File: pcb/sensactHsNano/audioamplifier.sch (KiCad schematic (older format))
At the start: 26 parts, among them U1 TAS5805M

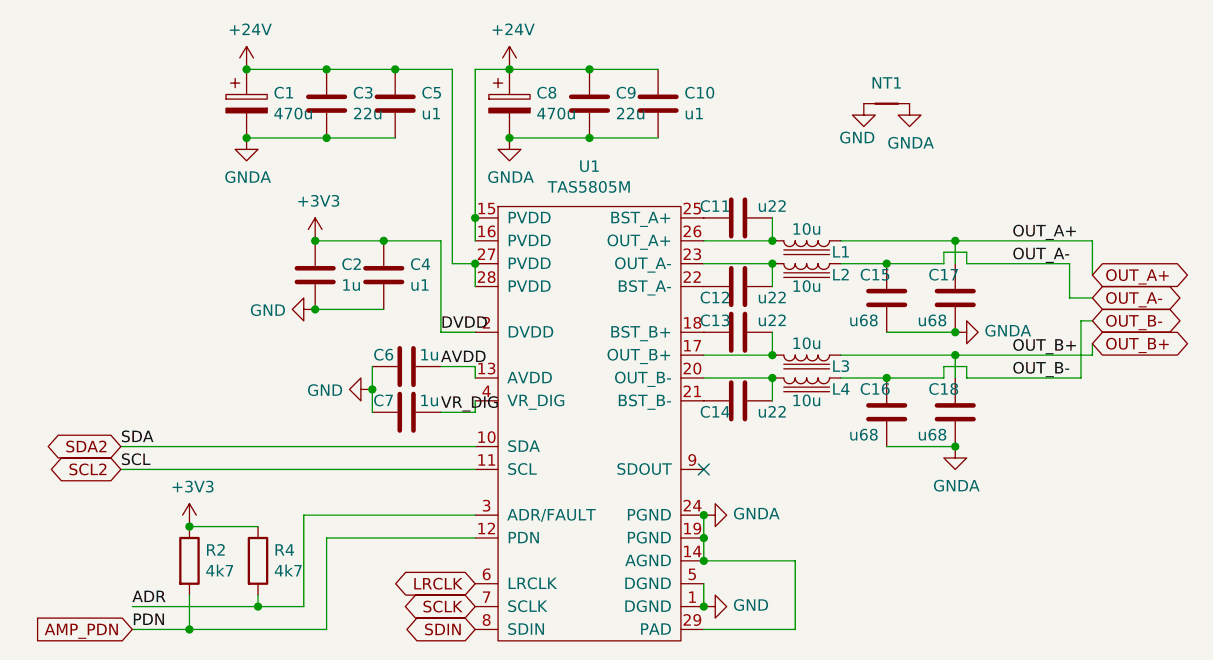
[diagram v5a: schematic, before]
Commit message: sensactHsNano for Reflow Soldering
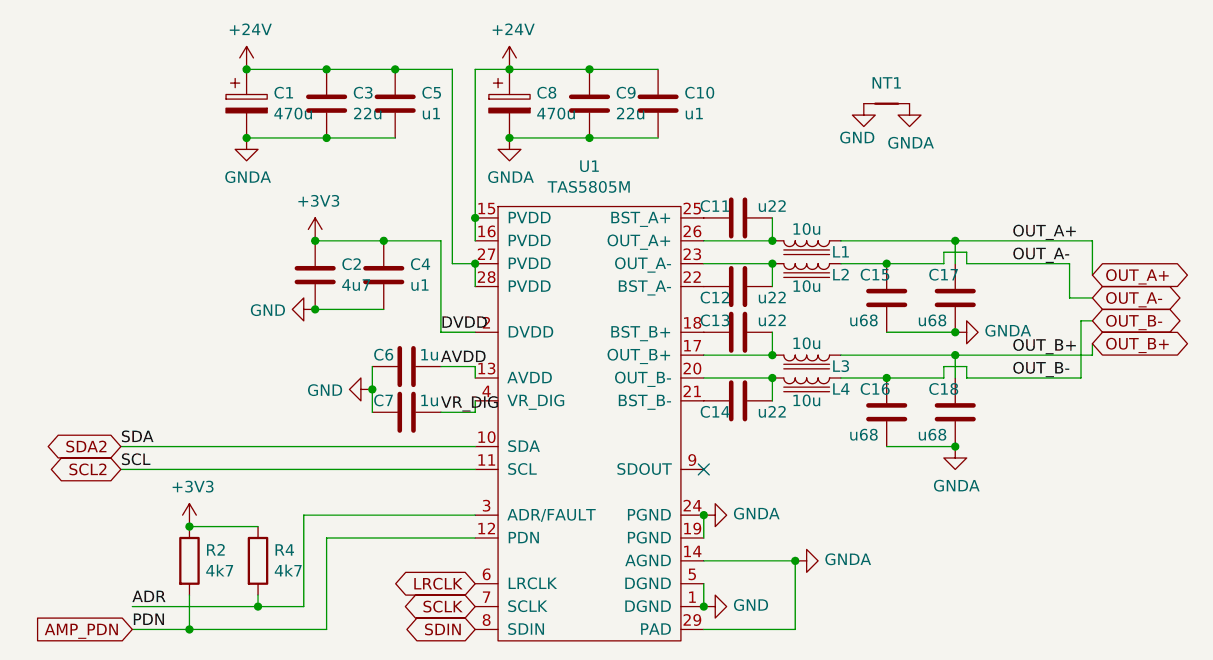
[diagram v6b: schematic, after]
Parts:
- removed U1: TAS5805M, sensact:TSSOP-28_4.4x9.7mm_Pitch0.65mm_pad_handsolder, symbol sensactHsNano-rescue:TAS5805M-sensact
- added U1: TAS5805M, Package_SO:HTSSOP-28-1EP_4.4x9.7mm_P0.65mm_EP2.85x5.4mm_ThermalVias, symbol liebler_SEMICONDUCTORS:TAS5805M
- C10, C11, C12, C13, C14, C4, C5, C6, C7: footprint Capacitor_SMD:C_0805_2012Metric_Pad1.18x1.45mm_HandSolder -> Capacitor_SMD:C_0603_1608Metric
- C2: value 1u -> 4u7; footprint Capacitor_SMD:C_0805_2012Metric_Pad1.18x1.45mm_HandSolder -> Capacitor_SMD:C_0603_1608Metric
- C3, C9: footprint Capacitor_SMD:C_1206_3216Metric_Pad1.33x1.80mm_HandSolder -> Capacitor_SMD:C_1206_3216Metric
- L1, L2, L3, L4: footprint liebler_PASSIVES:Inductor_CDRH104_handsolder -> liebler_PASSIVES:L_1040
- R4: footprint Resistor_SMD:R_0805_2012Metric_Pad1.20x1.40mm_HandSolder -> Resistor_SMD:R_0603_1608Metric
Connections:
- net +24V: now also U1.15 (PVDD), U1.16 (PVDD), U1.27 (PVDD), U1.28 (PVDD)
- net +3V3: now also U1.2 (DVDD)
- net ADR: now also U1.3 (ADR/FAULT)
- net AMP_PDN: now also U1.12 (PDN)
- net AVDD: now also U1.13 (AVDD)
- net GND: now also U1.1 (DGND), U1.5 (DGND)
- net GNDA: now also U1.14 (AGND), U1.19 (PGND), U1.24 (PGND), U1.29 (PAD)
- net LRCLK: now also U1.6 (LRCLK)
- net SCL2: now also U1.11 (SCL)
- net SCLK: now also U1.7 (SCLK)
- net SDA2: now also U1.10 (SDA)
- net SDIN: now also U1.8 (SDIN)
- net VR_DIG: now also U1.4 (VR_DIG)
- net at C11.1, L1.2: now also U1.26 (OUT_A+)
- net at C13.1, L3.2: now also U1.17 (OUT_B+)
- net at C13.2: now also U1.18 (BST_B+)
- net at C14.1, L4.2: now also U1.20 (OUT_B-)
- net at C14.2: now also U1.21 (BST_B-)
- net at C12.2: now also U1.22 (BST_A-)
- net at C12.1, L2.2: now also U1.23 (OUT_A-)
- net at C11.2: now also U1.25 (BST_A+)
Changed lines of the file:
@@
 F 0 "L1" V 5300 2300 50  0000 C CNN
 F 1 "10u" V 5200 2150 50  0000 C CNN
-F 2 "liebler_PASSIVES:Inductor_CDRH104_handsolder" H 5250 2150 50  0001 C CNN
+F 2 "liebler_PASSIVES:L_1040" H 5250 2150 50  0001 C CNN
 F 3 "~" H 5250 2150 50  0001 C CNN
 	1    5250 2150
 	0    1    1    0
-$EndComp
-$Comp
-L sensactHsNano-rescue:TAS5805M-sensact U1
-U 1 1 5F9CF512
-P 4300 2950
-F 0 "U1" H 4300 4075 50  0000 C CNN
-F 1 "TAS5805M" H 4300 3984 50  0000 C CNN
-F 2 "sensact:TSSOP-28_4.4x9.7mm_Pitch0.65mm_pad_handsolder" H 4300 3450 50  0001 C CNN
-F 3 "" H 4300 3450 50  0001 C CNN
-	1    4300 2950
-	1    0    0    -1
 $EndComp
 $Comp
@@
 F 0 "C11" V 4900 1950 50  0000 C CNN
 F 1 "u22" V 4900 2200 50  0000 C CNN
-F 2 "Capacitor_SMD:C_0805_2012Metric_Pad1.18x1.45mm_HandSolder" H 4988 1900 50  0001 C CNN
+F 2 "Capacitor_SMD:C_0603_1608Metric" H 4988 1900 50  0001 C CNN
 F 3 "~" H 4950 2050 50  0001 C CNN
 	1    4950 2050
@@
 F 0 "L2" V 5300 2400 50  0000 C CNN
 F 1 "10u" V 5350 2250 50  0000 C CNN
-F 2 "liebler_PASSIVES:Inductor_CDRH104_handsolder" H 5250 2250 50  0001 C CNN
+F 2 "liebler_PASSIVES:L_1040" H 5250 2250 50  0001 C CNN
 F 3 "~" H 5250 2250 50  0001 C CNN
 	1    5250 2250
@@
 F 0 "C12" V 5000 2250 50  0000 C CNN
 F 1 "u22" V 5000 2500 50  0000 C CNN
-F 2 "Capacitor_SMD:C_0805_2012Metric_Pad1.18x1.45mm_HandSolder" H 4988 2200 50  0001 C CNN
+F 2 "Capacitor_SMD:C_0603_1608Metric" H 4988 2200 50  0001 C CNN
 F 3 "~" H 4950 2350 50  0001 C CNN
 	1    4950 2350
@@
 F 0 "L3" V 5300 2800 50  0000 C CNN
 F 1 "10u" V 5200 2650 50  0000 C CNN
-F 2 "liebler_PASSIVES:Inductor_CDRH104_handsolder" H 5250 2650 50  0001 C CNN
+F 2 "liebler_PASSIVES:L_1040" H 5250 2650 50  0001 C CNN
 F 3 "~" H 5250 2650 50  0001 C CNN
 	1    5250 2650
@@
 F 0 "C13" V 4900 2450 50  0000 C CNN
 F 1 "u22" V 4900 2700 50  0000 C CNN
-F 2 "Capacitor_SMD:C_0805_2012Metric_Pad1.18x1.45mm_HandSolder" H 4988 2400 50  0001 C CNN
+F 2 "Capacitor_SMD:C_0603_1608Metric" H 4988 2400 50  0001 C CNN
 F 3 "~" H 4950 2550 50  0001 C CNN
 	1    4950 2550
@@
 F 0 "L4" V 5300 2900 50  0000 C CNN
 F 1 "10u" V 5350 2750 50  0000 C CNN
-F 2 "liebler_PASSIVES:Inductor_CDRH104_handsolder" H 5250 2750 50  0001 C CNN
+F 2 "liebler_PASSIVES:L_1040" H 5250 2750 50  0001 C CNN
 F 3 "~" H 5250 2750 50  0001 C CNN
 	1    5250 2750
@@
 F 0 "C14" V 5000 2750 50  0000 C CNN
 F 1 "u22" V 5000 3000 50  0000 C CNN
-F 2 "Capacitor_SMD:C_0805_2012Metric_Pad1.18x1.45mm_HandSolder" H 4988 2700 50  0001 C CNN
+F 2 "Capacitor_SMD:C_0603_1608Metric" H 4988 2700 50  0001 C CNN
 F 3 "~" H 4950 2850 50  0001 C CNN
 	1    4950 2850
@@
 	5100 2850 5100 2750
 Connection ~ 5100 2750
-$Comp
-L Device:C C15
-U 1 1 5F9D60B0
-P 5600 2400
-F 0 "C15" H 5650 2300 50  0000 C CNN
-F 1 "u68" H 5700 2500 50  0000 C CNN
-F 2 "Capacitor_SMD:C_1206_3216Metric_Pad1.33x1.80mm_HandSolder" H 5638 2250 50  0001 C CNN
-F 3 "~" H 5600 2400 50  0001 C CNN
-	1    5600 2400
-	-1   0    0    1
-$EndComp
-$Comp
-L Device:C C17
-U 1 1 5F9D6EDC
-P 5900 2400
-F 0 "C17" H 5950 2300 50  0000 C CNN
-F 1 "u68" H 6000 2500 50  0000 C CNN
-F 2 "Capacitor_SMD:C_1206_3216Metric_Pad1.33x1.80mm_HandSolder" H 5938 2250 50  0001 C CNN
-F 3 "~" H 5900 2400 50  0001 C CNN
-	1    5900 2400
-	-1   0    0    1
-$EndComp
 Wire Wire Line
 	5400 2250 5600 2250
@@
 Wire Wire Line
 	5600 2550 5900 2550
-$Comp
-L Device:C C16
-U 1 1 5F9D93BD
-P 5600 2900
-F 0 "C16" H 5650 2800 50  0000 C CNN
-F 1 "u68" H 5700 3000 50  0000 C CNN
-F 2 "Capacitor_SMD:C_1206_3216Metric_Pad1.33x1.80mm_HandSolder" H 5638 2750 50  0001 C CNN
-F 3 "~" H 5600 2900 50  0001 C CNN
-	1    5600 2900
-	-1   0    0    1
-$EndComp
-$Comp
-L Device:C C18
-U 1 1 5F9D93C7
-P 5900 2900
-F 0 "C18" H 5950 2800 50  0000 C CNN
-F 1 "u68" H 6000 3000 50  0000 C CNN
-F 2 "Capacitor_SMD:C_1206_3216Metric_Pad1.33x1.80mm_HandSolder" H 5938 2750 50  0001 C CNN
-F 3 "~" H 5900 2900 50  0001 C CNN
-	1    5900 2900
-	-1   0    0    1
-$EndComp
 Wire Wire Line
 	5400 2750 5600 2750
@@
 	5600 3050 5900 3050
 NoConn ~ 4800 3150
-Connection ~ 4800 3750
 Wire Wire Line
 	4800 3750 4800 3650
@@
 F 0 "C3" H 3265 1596 50  0000 L CNN
 F 1 "22u" H 3265 1505 50  0000 L CNN
-F 2 "Capacitor_SMD:C_1206_3216Metric_Pad1.33x1.80mm_HandSolder" H 3188 1400 50  0001 C CNN
+F 2 "Capacitor_SMD:C_1206_3216Metric" H 3188 1400 50  0001 C CNN
 F 3 "~" H 3150 1550 50  0001 C CNN
 	1    3150 1550
@@
 F 0 "C5" H 3565 1596 50  0000 L CNN
 F 1 "u1" H 3565 1505 50  0000 L CNN
-F 2 "Capacitor_SMD:C_0805_2012Metric_Pad1.18x1.45mm_HandSolder" H 3488 1400 50  0001 C CNN
+F 2 "Capacitor_SMD:C_0603_1608Metric" H 3488 1400 50  0001 C CNN
 F 3 "~" H 3450 1550 50  0001 C CNN
 	1    3450 1550
@@
 F 0 "C9" H 4415 1596 50  0000 L CNN
 F 1 "22u" H 4415 1505 50  0000 L CNN
-F 2 "Capacitor_SMD:C_1206_3216Metric_Pad1.33x1.80mm_HandSolder" H 4338 1400 50  0001 C CNN
+F 2 "Capacitor_SMD:C_1206_3216Metric" H 4338 1400 50  0001 C CNN
 F 3 "~" H 4300 1550 50  0001 C CNN
 	1    4300 1550
@@
 F 0 "C10" H 4715 1596 50  0000 L CNN
 F 1 "u1" H 4715 1505 50  0000 L CNN
-F 2 "Capacitor_SMD:C_0805_2012Metric_Pad1.18x1.45mm_HandSolder" H 4638 1400 50  0001 C CNN
+F 2 "Capacitor_SMD:C_0603_1608Metric" H 4638 1400 50  0001 C CNN
 F 3 "~" H 4600 1550 50  0001 C CNN
 	1    4600 1550
@@
 	4300 1700 3950 1700
 Wire Wire Line
-	3800 2150 3800 2050
-Wire Wire Line
 	3800 2350 3800 2250
 Wire Wire Line
@@
 P 3100 2300
 F 0 "C2" H 3215 2346 50  0000 L CNN
-F 1 "1u" H 3215 2255 50  0000 L CNN
-F 2 "Capacitor_SMD:C_0805_2012Metric_Pad1.18x1.45mm_HandSolder" H 3138 2150 50  0001 C CNN
+F 1 "4u7" H 3215 2255 50  0000 L CNN
+F 2 "Capacitor_SMD:C_0603_1608Metric" H 3138 2150 50  0001 C CNN
 F 3 "~" H 3100 2300 50  0001 C CNN
 	1    3100 2300
@@
 F 0 "C4" H 3515 2346 50  0000 L CNN
 F 1 "u1" H 3515 2255 50  0000 L CNN
-F 2 "Capacitor_SMD:C_0805_2012Metric_Pad1.18x1.45mm_HandSolder" H 3438 2150 50  0001 C CNN
+F 2 "Capacitor_SMD:C_0603_1608Metric" H 3438 2150 50  0001 C CNN
 F 3 "~" H 3400 2300 50  0001 C CNN
 	1    3400 2300
@@
 	3400 2450 3100 2450
 Wire Wire Line
-	3800 2050 3800 1400
-Wire Wire Line
 	3800 1400 3950 1400
-Connection ~ 3800 2050
 Wire Wire Line
 	3700 2250 3800 2250
 Wire Wire Line
 	3700 1400 3700 2250
-Connection ~ 3800 2250
 $Comp
 L power:GND #PWR06
@@
 F 0 "C6" V 3450 2600 50  0000 C CNN
 F 1 "1u" V 3450 2800 50  0000 C CNN
-F 2 "Capacitor_SMD:C_0805_2012Metric_Pad1.18x1.45mm_HandSolder" H 3538 2550 50  0001 C CNN
+F 2 "Capacitor_SMD:C_0603_1608Metric" H 3538 2550 50  0001 C CNN
 F 3 "~" H 3500 2700 50  0001 C CNN
 	1    3500 2700
@@
 F 0 "C7" V 3450 2800 50  0000 C CNN
 F 1 "1u" V 3450 3000 50  0000 C CNN
-F 2 "Capacitor_SMD:C_0805_2012Metric_Pad1.18x1.45mm_HandSolder" H 3538 2750 50  0001 C CNN
+F 2 "Capacitor_SMD:C_0603_1608Metric" H 3538 2750 50  0001 C CNN
 F 3 "~" H 3500 2900 50  0001 C CNN
 	1    3500 2900
@@
 F 0 "R4" H 2920 3596 50  0000 L CNN
 F 1 "4k7" H 2920 3505 50  0000 L CNN
-F 2 "Resistor_SMD:R_0805_2012Metric_Pad1.20x1.40mm_HandSolder" V 2780 3550 50  0001 C CNN
+F 2 "Resistor_SMD:R_0603_1608Metric" V 2780 3550 50  0001 C CNN
 F 3 "~" H 2850 3550 50  0001 C CNN
 	1    2850 3550
@@
 	0    -1   -1   0
 $EndComp
-Wire Wire Line
-	4800 3550 4800 3450
-Connection ~ 4800 3350
-Connection ~ 4800 3450
-Wire Wire Line
-	4800 3450 4800 3350
 $Comp
 L power:GNDA #PWR058
@@
 Wire Wire Line
 	5200 3550 4800 3550
-Connection ~ 4800 3550
+Wire Wire Line
+	3800 1400 3800 2050
+Wire Wire Line
+	4800 3350 4800 3450
+$Comp
+L liebler_SEMICONDUCTORS:TAS5805M U1
+U 1 1 61306266
+P 4300 2950
+F 0 "U1" H 4300 4075 50  0000 C CNN
+F 1 "TAS5805M" H 4300 3984 50  0000 C CNN
+F 2 "Package_SO:HTSSOP-28-1EP_4.4x9.7mm_P0.65mm_EP2.85x5.4mm_ThermalVias" H 4300 3450 50  0001 C CNN
+F 3 "" H 4300 3450 50  0001 C CNN
+	1    4300 2950
+	1    0    0    -1
+$EndComp
+Connection ~ 4800 3750
+Connection ~ 4800 3350
+Connection ~ 3800 2250
+Wire Wire Line
+	3800 2150 3800 2050
+Connection ~ 3800 2050
+$Comp
+L Device:C C18
+U 1 1 5F9D93C7
+P 5900 2900
+F 0 "C18" H 5950 2800 50  0000 C CNN
+F 1 "u68" H 6000 3000 50  0000 C CNN
+F 2 "Capacitor_SMD:C_1206_3216Metric_Pad1.33x1.80mm_HandSolder" H 5938 2750 50  0001 C CNN
+F 3 "~" H 5900 2900 50  0001 C CNN
+	1    5900 2900
+	-1   0    0    1
+$EndComp
+$Comp
+L Device:C C16
+U 1 1 5F9D93BD
+P 5600 2900
+F 0 "C16" H 5650 2800 50  0000 C CNN
+F 1 "u68" H 5700 3000 50  0000 C CNN
+F 2 "Capacitor_SMD:C_1206_3216Metric_Pad1.33x1.80mm_HandSolder" H 5638 2750 50  0001 C CNN
+F 3 "~" H 5600 2900 50  0001 C CNN
+	1    5600 2900
+	-1   0    0    1
+$EndComp
+$Comp
+L Device:C C17
+U 1 1 5F9D6EDC
+P 5900 2400
+F 0 "C17" H 5950 2300 50  0000 C CNN
+F 1 "u68" H 6000 2500 50  0000 C CNN
+F 2 "Capacitor_SMD:C_1206_3216Metric_Pad1.33x1.80mm_HandSolder" H 5938 2250 50  0001 C CNN
+F 3 "~" H 5900 2400 50  0001 C CNN
+	1    5900 2400
+	-1   0    0    1
+$EndComp
+$Comp
+L Device:C C15
+U 1 1 5F9D60B0
+P 5600 2400
+F 0 "C15" H 5650 2300 50  0000 C CNN
+F 1 "u68" H 5700 2500 50  0000 C CNN
+F 2 "Capacitor_SMD:C_1206_3216Metric_Pad1.33x1.80mm_HandSolder" H 5638 2250 50  0001 C CNN
+F 3 "~" H 5600 2400 50  0001 C CNN
+	1    5600 2400
+	-1   0    0    1
+$EndComp
+$Comp
+L power:GNDA #PWR0110
+U 1 1 6132B463
+P 5200 3550
+F 0 "#PWR0110" H 5200 3300 50  0001 C CNN
+F 1 "GNDA" V 5205 3422 50  0000 R CNN
+F 2 "" H 5200 3550 50  0001 C CNN
+F 3 "" H 5200 3550 50  0001 C CNN
+	1    5200 3550
+	0    -1   -1   0
+$EndComp
+Connection ~ 5200 3550
 $EndSCHEMATC
